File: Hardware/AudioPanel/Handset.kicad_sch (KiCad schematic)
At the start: 1 part, among them J3 8P8C_Shielded

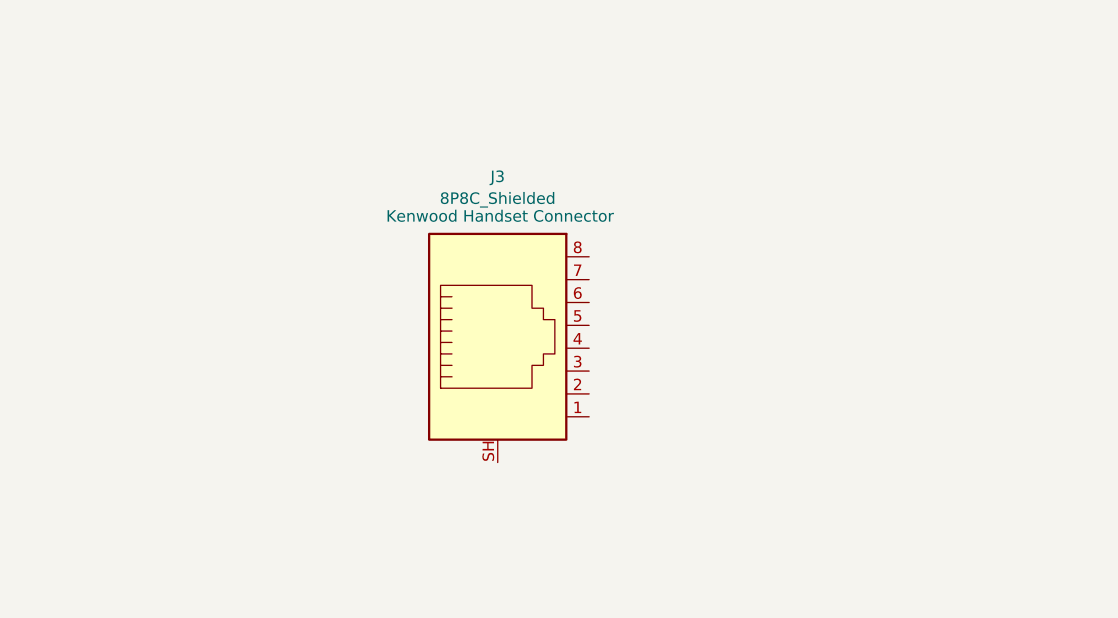
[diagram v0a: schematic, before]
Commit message: Added crosspoints for each connector
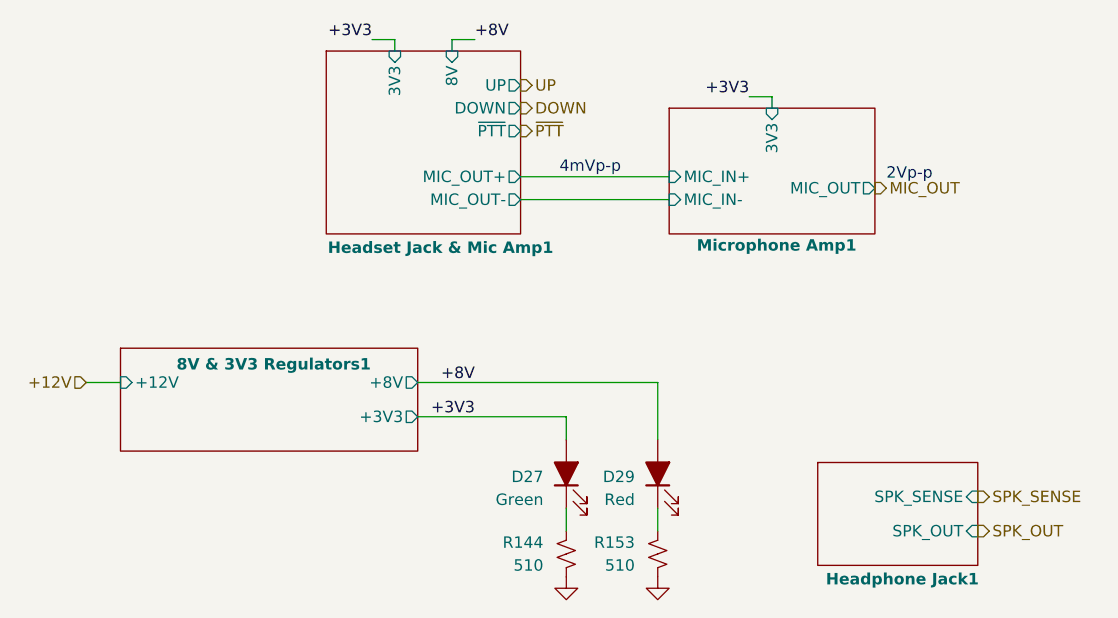
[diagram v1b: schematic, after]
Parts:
- removed J3: 8P8C_Shielded, symbol Connector:8P8C_Shielded
- added D27: Green, LED_THT:LED_D5.0mm, symbol Device:LED_Filled
- added D29: Red, LED_THT:LED_D5.0mm, symbol Device:LED_Filled
- added R144, R153: 510, Resistor_SMD:R_0603_1608Metric_Pad0.98x0.95mm_HandSolder, symbol Device:R_Small_US
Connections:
- new net: D27.1 (K), R144.2
- new net: D29.1 (K), R153.2
- new net +3V3: D27.2 (A)
- new net +8V: D29.2 (A)
- new net GND: R144.1, R153.1
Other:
- added sheet 8V & 3V3 Regulators1 (12-8-3Reg.kicad_sch)
- added sheet Headphone Jack1 (HeadphoneJack.kicad_sch)
- added sheet Headset Jack & Mic Amp1 (HandsetJackAmp.kicad_sch)
- added sheet Microphone Amp1 (MicAmp.kicad_sch)
- note added: "2Vp-p"
- note added: "4mVp-p"
